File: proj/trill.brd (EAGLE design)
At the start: 58.4 x 120.1 mm, 127 parts, among them J1 SPKRAST_01532MR, J2 MICCMA-4544PF-W, J3 ADAFRUIT_OLED_13, J4 DM3D-SFDM, J5 SJ1-3523N, J6 CONUFL001, M1 Z3OC_VIB_MOTOR, U1 SIM5300EA, U10 3.3V 600mA, U11 MCP1642B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

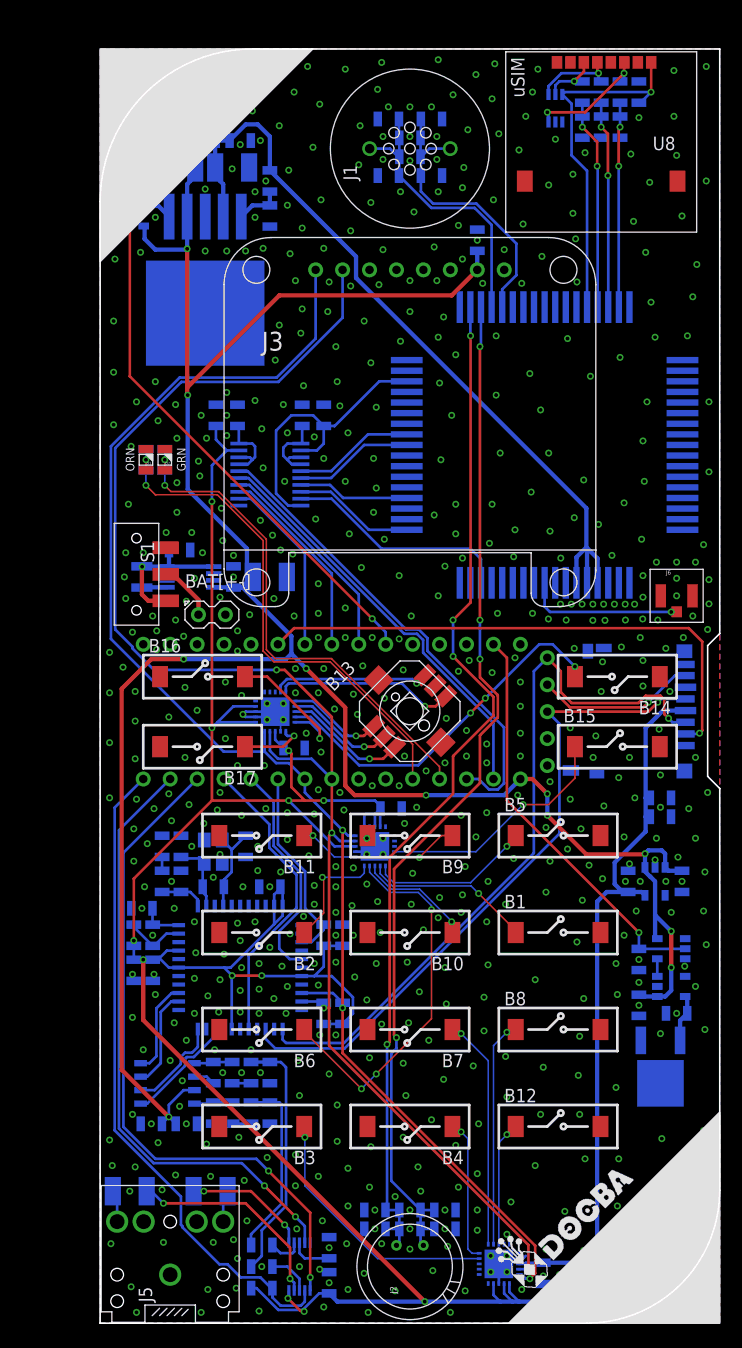
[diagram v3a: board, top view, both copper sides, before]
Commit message: Cleaned up repo Added raccoon artwork to Trill board
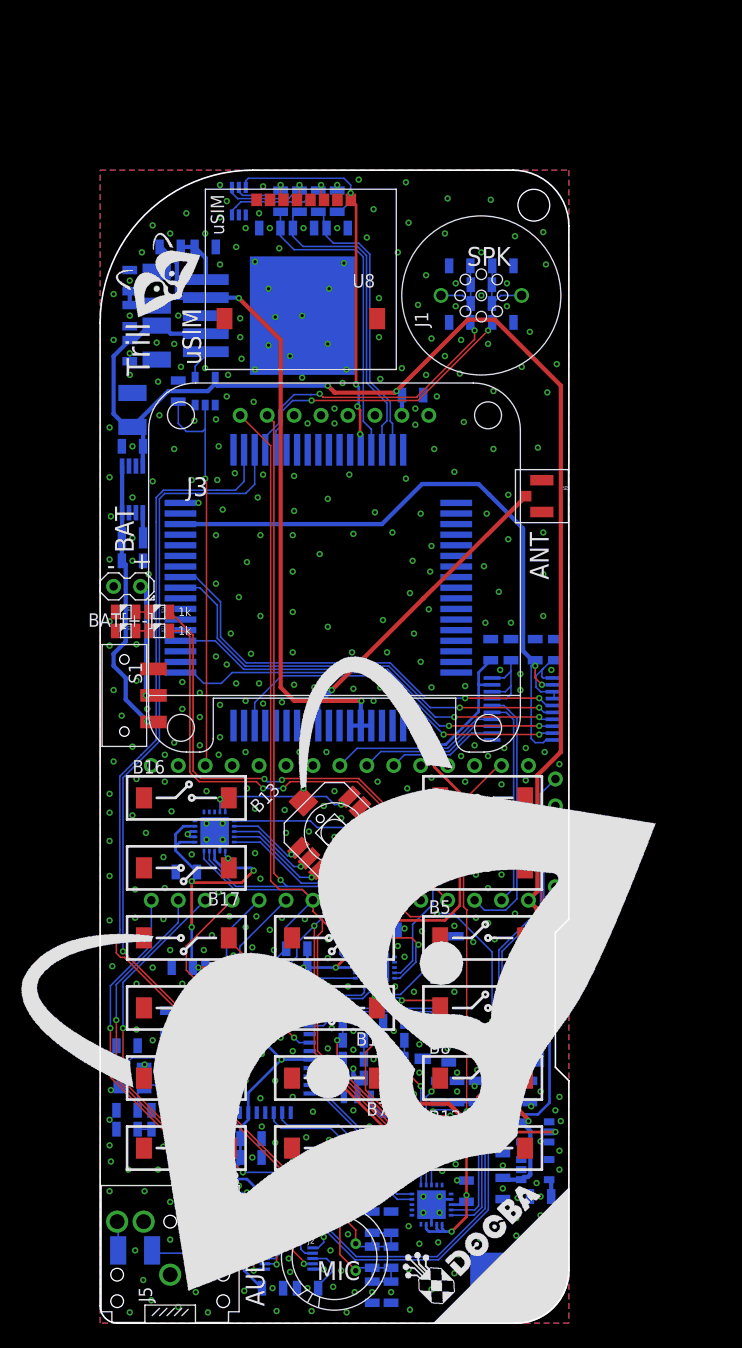
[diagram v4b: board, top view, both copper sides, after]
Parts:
- moved C31 34.7 mm to (31.9, 21.8), turned to 90 degrees
- moved C2 34.1 mm to (36.8, 63.5)
- moved R1 34.0 mm to (38.7, 63.5)
- moved R2 32.5 mm to (42.9, 63.5)
- moved U6 32.5 mm to (39.9, 57.9)
- moved C32 32.2 mm to (33.7, 21.8), turned to 90 degrees
- moved U8 31.1 mm to (18.9, 105.9)
- moved U9 31.1 mm to (13.1, 105.8)
- moved C7 31.0 mm to (16.0, 103.3), turned to 180 degrees
- moved J4 30.6 mm to (39.9, 30.5)
- moved R8 30.3 mm to (18.8, 105.8)
- moved R9 30.3 mm to (17.0, 105.8)
- moved C10 30.3 mm to (22.4, 105.8)
- moved R7 30.3 mm to (20.6, 105.8)
- moved C1 29.8 mm to (41.0, 63.5)
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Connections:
- net !STA013_RST: now also N1.26; no longer N1.25
- net AMP_SHUTDOWN: now also N1.29; no longer N1.30
- net AMP_VOL_CLK: now also N1.28; no longer N1.29
- net AMP_VOL_UPDN: now also N1.30; no longer N1.28
- net GSM_PWR_EN: now also N1.3; no longer N1.10
- net GSM_PWR_KEY: now also N1.9; no longer N1.8
- net GSM_RING: now also N1.8; no longer N1.9
- net GSM_STATUS: now also N1.10; no longer N1.7
- net MICROSD_CS: now also N1.21; no longer N1.6
- net N$1: now also U3.10; no longer U3.9
- net N$2: now also U3.12; no longer U3.11
- net N$3: now also U3.13; no longer U3.12
- net N$4: now also U3.14; no longer U3.13
- net N$5: now also U3.11; no longer U3.10
- net N$6: now also U3.15; no longer U3.14
- net N$7: now also U3.9; no longer U3.15
- net STA013_DREQ: now also N1.25; no longer N1.26
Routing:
- net 3.3V: track 311.5 -> 210.4 mm, vias 12 -> 18
- net 5.0V: track 235.1 -> 179.1 mm, vias 11 -> 5
- net N$22: track 27.9 -> 62.2 mm, vias 0 -> 2
- net I2C_SCL: track 147.4 -> 116.6 mm, vias 4 -> 3
- net N$27: track 11.4 -> 42.2 mm, vias 0 -> 2
- net N$26: track 11.3 -> 41.9 mm, vias 0 -> 2
- net AOUT_L: track 19.2 -> 48.9 mm, vias 0 -> 2
- net MICROSD_CS: track 51.3 -> 23.4 mm, vias 1 -> 3
- net N$25: track 10.5 -> 38.3 mm, vias 0 -> 2
- net N$24: track 11.5 -> 38.2 mm, vias 0 -> 2
- net AOUT_R: track 25.4 -> 51.8 mm, vias 0 -> 2
- net AMP_VOL_UPDN: track 64.0 -> 43.2 mm
- net GSM_RXD: track 45.2 -> 24.7 mm
- net GSM_TXD: track 39.6 -> 19.8 mm
- net SPI_MOSI: track 69.2 -> 49.6 mm, vias 1 -> 0
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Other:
- board size 58.4 x 120.1 mm -> 44.2 x 108.7 mm
- board text added: "+"
- board text added: "-"
- board text added: "ANT"
- board text added: "AUDIO"
- board text added: "BAT"
- board text added: "ESDA"
- board text added: "MIC"
- board text added: "SPK"
- board text added: "STA013"
- board text added: "Trill"
- board text added: "uSIM"
- board text removed: "14.7456 XTAL"
- board text removed: "ESDA6V1"
- board text removed: "GRN"
- board text removed: "ORN"

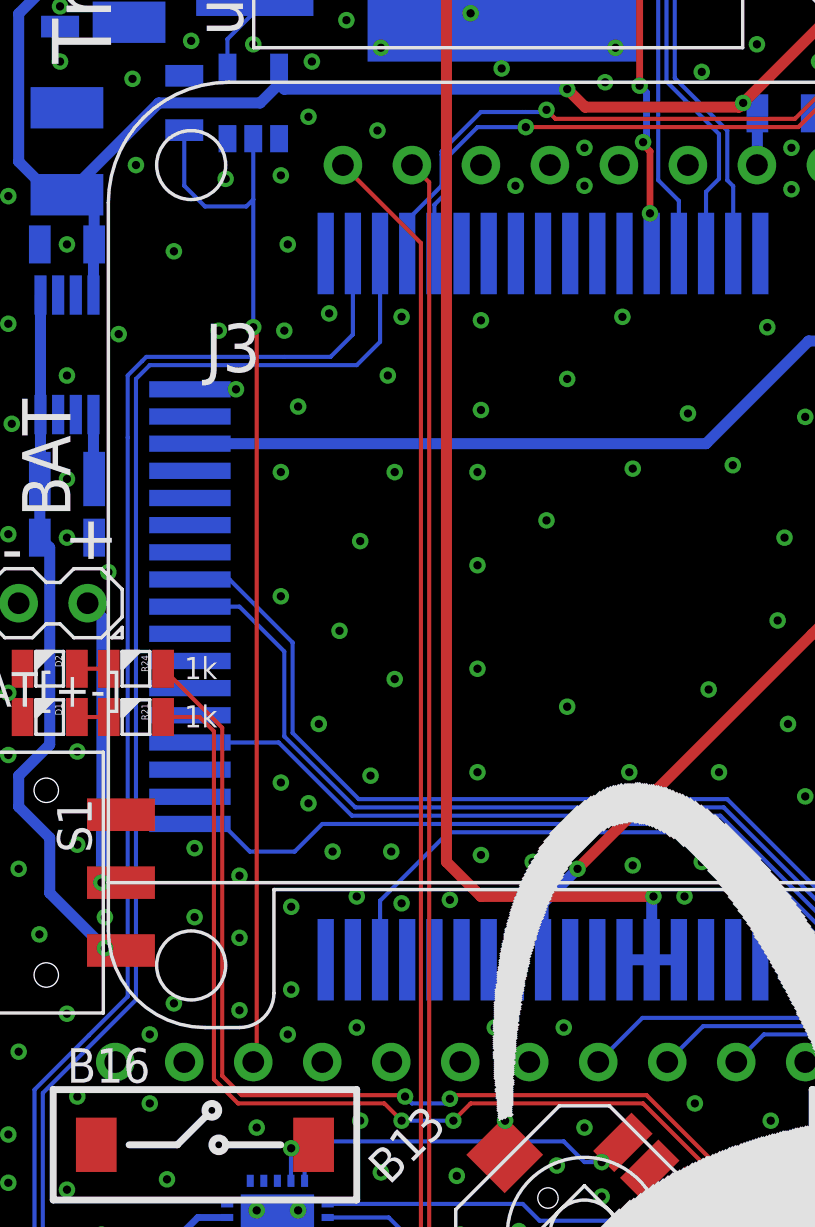
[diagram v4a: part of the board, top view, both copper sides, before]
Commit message: Added OLED RESET line on Trill board
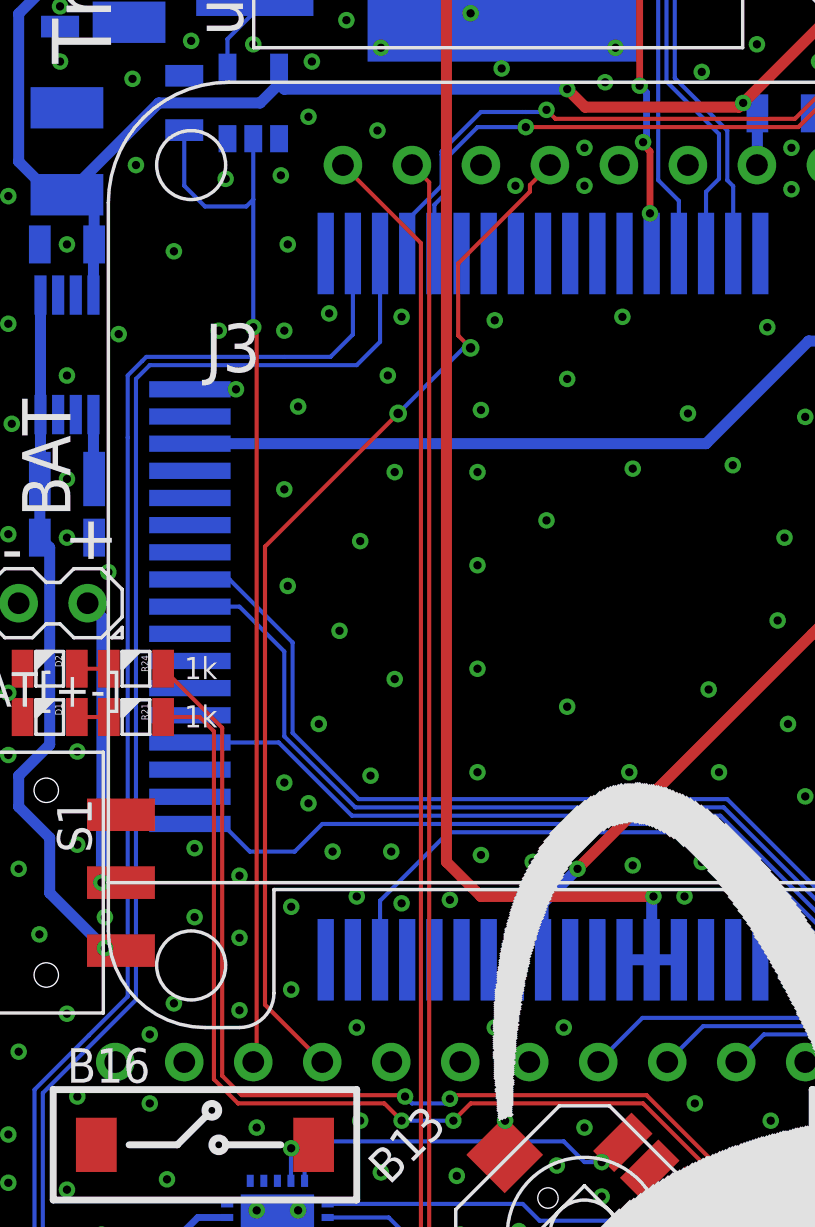
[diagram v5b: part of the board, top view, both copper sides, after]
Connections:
- new net OLED_RST: J3.RST, N1.4
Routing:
- net OLED_RST: track 0.00 -> 38.8 mm, vias 0 -> 2
- net GND: vias 493 -> 492
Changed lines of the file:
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@@
 <?xml version="1.0" encoding="utf-8"?>
 <!DOCTYPE eagle SYSTEM "eagle.dtd">
-<eagle version="8.4.0">
+<eagle version="8.4.1">
 <drawing>
 <settings>
@@
 <setting verticaltext="up"/>
 </settings>
-<grid distance="2" unitdist="mil" unit="mil" style="lines" multiple="1" display="yes" altdistance="0.025" altunitdist="inch" altunit="inch"/>
+<grid distance="0.005" unitdist="inch" unit="inch" style="lines" multiple="1" display="yes" altdistance="0.025" altunitdist="inch" altunit="inch"/>
 <layers>
 <layer number="1" name="Top" color="4" fill="1" visible="yes" active="yes"/>
@@
 <param name="dpMaxLengthDifference" value="10mm"/>
 <param name="dpGapFactor" value="2.5"/>
+<param name="checkAngle" value="0"/>
 <param name="checkFont" value="1"/>
 <param name="checkRestrict" value="0"/>
@@
 <via x="9.271" y="77.343" extent="1-16" drill="0.3048"/>
 <via x="11.557" y="76.708" extent="1-16" drill="0.3048"/>
-<via x="18.288" y="79.883" extent="1-16" drill="0.3048"/>
+<via x="18.796" y="79.883" extent="1-16" drill="0.3048"/>
 <via x="6.985" y="82.423" extent="1-16" drill="0.3048"/>
 <via x="11.176" y="82.677" extent="1-16" drill="0.3048"/>
@@
 <via x="7.747" y="57.912" extent="1-16" drill="0.3048"/>
 <via x="7.747" y="60.452" extent="1-16" drill="0.3048"/>
-<via x="10.922" y="74.295" extent="1-16" drill="0.3048"/>
+<via x="11.049" y="73.66" extent="1-16" drill="0.3048"/>
 <via x="15.113" y="74.295" extent="1-16" drill="0.3048"/>
-<via x="10.922" y="69.723" extent="1-16" drill="0.3048"/>
+<via x="11.176" y="70.104" extent="1-16" drill="0.3048"/>
 <via x="12.319" y="65.024" extent="1-16" drill="0.3048"/>
 <via x="14.224" y="63.119" extent="1-16" drill="0.3048"/>
@@
 <via x="41.783" y="66.675" extent="1-16" drill="0.3048"/>
 <via x="41.783" y="70.612" extent="1-16" drill="0.3048"/>
-<via x="10.922" y="62.865" extent="1-16" drill="0.3048"/>
+<via x="11.049" y="62.865" extent="1-16" drill="0.3048"/>
 <via x="11.938" y="62.103" extent="1-16" drill="0.3048"/>
 <via x="12.827" y="60.325" extent="1-16" drill="0.3048"/>
@@
 <via x="9.398" y="54.483" extent="1-16" drill="0.3048"/>
 <via x="11.303" y="55.245" extent="1-16" drill="0.3048"/>
-<via x="11.176" y="53.594" extent="1-16" drill="0.3048"/>
 <via x="13.716" y="53.848" extent="1-16" drill="0.3048"/>
 <via x="18.796" y="53.848" extent="1-16" drill="0.3048"/>
@@
 <wire x1="15.09958125" y1="45.355" x2="18.97358125" y2="41.481" width="0.1524" layer="16"/>
 </signal>
+<signal name="OLED_RST">
+<contactref element="J3" pad="RST"/>
+<contactref element="N1" pad="4"/>
+<wire x1="20.828" y1="85.598" x2="20.0914" y2="84.8614" width="0.1524" layer="1"/>
+<wire x1="20.0914" y1="84.8614" x2="20.0914" y2="84.61505625" width="0.1524" layer="1"/>
+<wire x1="20.0914" y1="84.61505625" x2="17.4498" y2="81.97345625" width="0.1524" layer="1"/>
+<wire x1="17.4498" y1="79.3242" x2="17.907" y2="78.867" width="0.1524" layer="1"/>
+<via x="17.907" y="78.867" extent="1-16" drill="0.35"/>
+<wire x1="17.4498" y1="81.97345625" x2="17.4498" y2="79.3242" width="0.1524" layer="1"/>
+<wire x1="17.907" y1="78.867" x2="17.653" y2="78.867" width="0.1524" layer="16"/>
+<wire x1="17.653" y1="78.867" x2="15.24" y2="76.454" width="0.1524" layer="16"/>
+<via x="15.24" y="76.454" extent="1-16" drill="0.35"/>
+<wire x1="15.24" y1="76.454" x2="10.3378" y2="71.5518" width="0.1524" layer="1"/>
+<wire x1="10.3378" y1="54.6862" x2="12.446" y2="52.578" width="0.1524" layer="1"/>
+<wire x1="10.3378" y1="71.5518" x2="10.3378" y2="54.6862" width="0.1524" layer="1"/>
+</signal>
 </signals>
